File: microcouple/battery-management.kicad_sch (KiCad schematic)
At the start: 17 parts, among them Q1 AO3415, SW2 SW_SPDT_MSK12CO2, U3 MCP73831-2-OT, U4 LM3671MFX

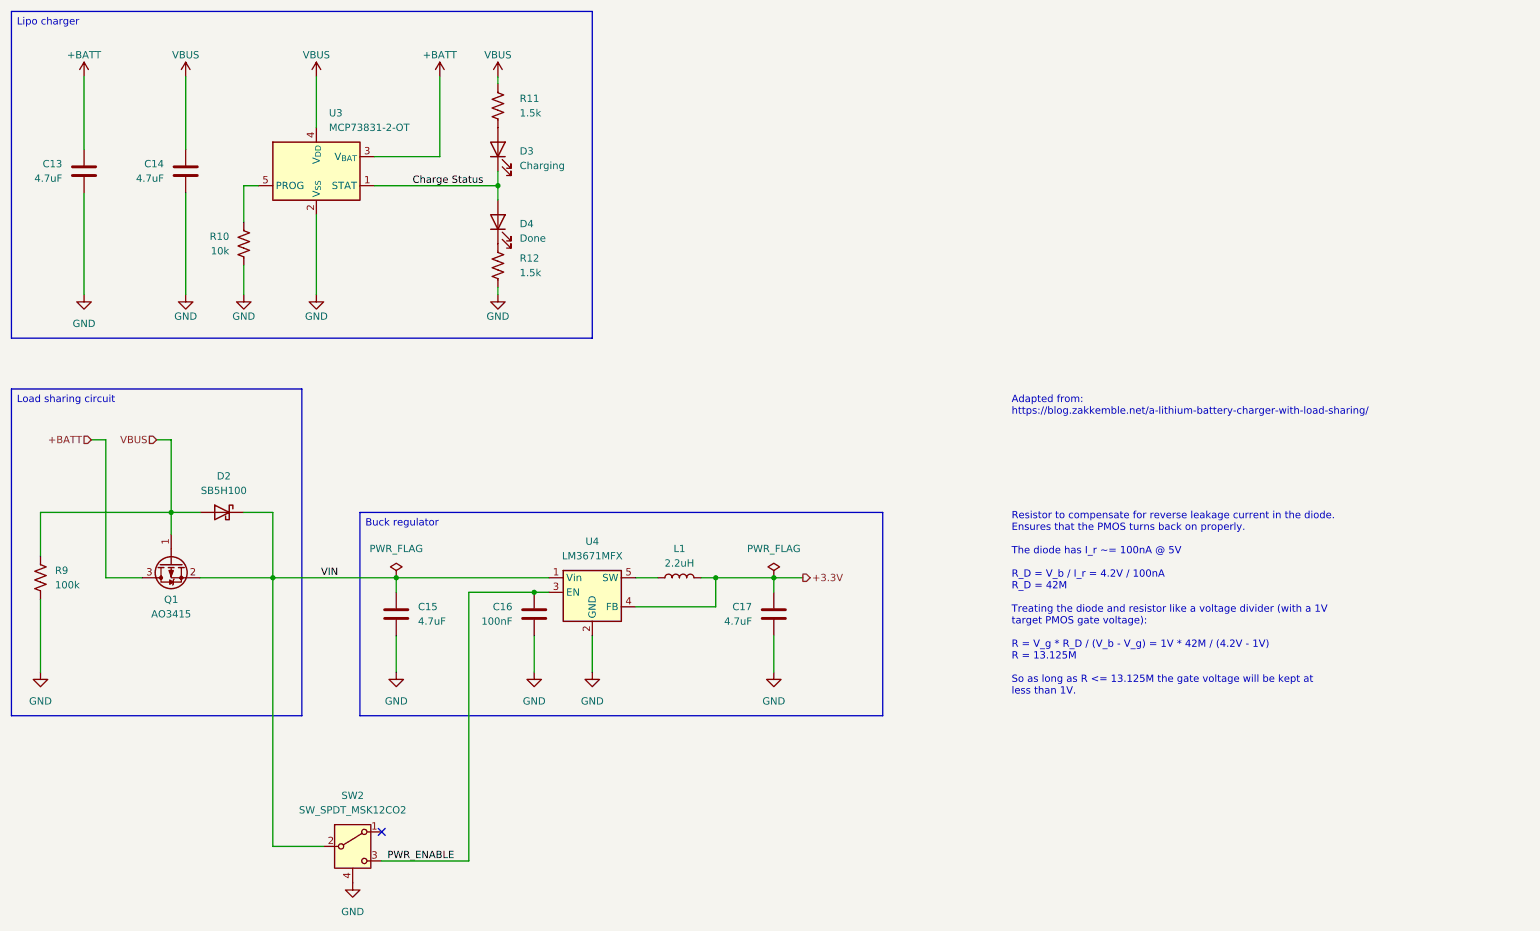
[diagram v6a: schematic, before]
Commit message: Update for JLCPCB
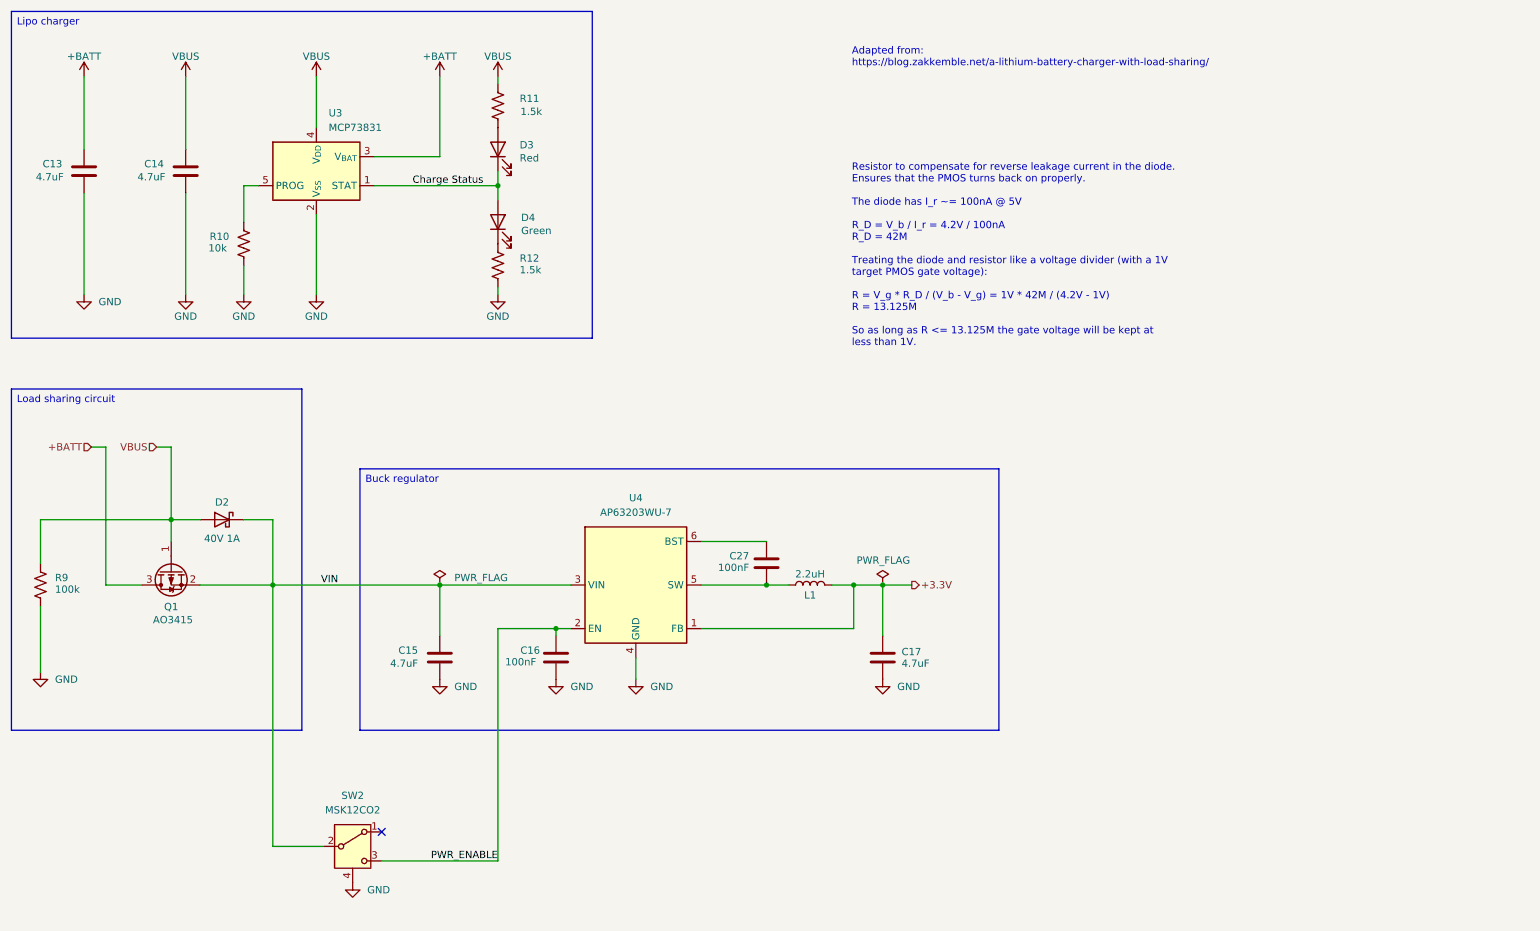
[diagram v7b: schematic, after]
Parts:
- added C27: 100nF, GS_Capacitors:C_0201_0603Metric, symbol GS_Capacitor_0201:C_0201_100nF
- C13, C14, C15, C17: footprint GS_SMD:0402_1005Metric -> GS_Capacitors:C_0402_1005Metric; symbol Device:C -> GS_Capacitor_0402:C_0402_4.7uF; LCSC ID (none) -> C76996; Manufacturer (none) -> Murata Electronics; Mfr. Part # (none) -> GRM155R60J475ME87D; Package (none) -> 0402
- C16: footprint GS_SMD:0201_0603Metric -> GS_Capacitors:C_0201_0603Metric; symbol Device:C -> GS_Capacitor_0201:C_0201_100nF; LCSC ID (none) -> C18164587; Manufacturer (none) -> CCTC; Mfr. Part # (none) -> TCC0201X5R104M250ZT; Package (none) -> 0201
- D2: value SB5H100 -> 40V 1A; footprint Diode_SMD:D_SMB -> Diode_SMD:D_SOD-123; symbol Diode:SB5H100 -> GS_Diodes:1N5819W; LCSC ID (none) -> C41431973; Manufacturer (none) -> GOODWORK; Mfr. Part # (none) -> 1N5819W; Package (none) -> SOD-123
- D3: value Charging -> Red; symbol Device:LED -> GS_Optoelectronic:LED_0201_Red; LCSC ID (none) -> C3646923; Manufacturer (none) -> XINGLIGHT; Mfr. Part # (none) -> XL-0201SURC; Package (none) -> 0201
- D4: value Done -> Green; symbol Device:LED -> GS_Optoelectronic:LED_0201_Green; LCSC ID (none) -> C3646922; Manufacturer (none) -> XINGLIGHT; Mfr. Part # (none) -> XL-0201UGC; Package (none) -> 0201
- L1: symbol Device:L -> GS_Inductors:L_1008_2.2uH; LCSC ID (none) -> C19634045; Manufacturer (none) -> APV; Mfr. Part # (none) -> PNR252012-2R2M; Package (none) -> 1008
- Q1: symbol Transistor_FET:AO3401A -> GS_Transistors:MOSFET_P-Ch_20V_4.8A_37mR; LCSC ID (none) -> C840839; Manufacturer (none) -> MDD(Microdiode Semiconductor); Mfr. Part # (none) -> AO3415; Package (none) -> SOT-23
- R10: footprint GS_SMD:0201_0603Metric -> GS_Resistors:R_0201_0603Metric; symbol Device:R_US -> GS_Resistor_0201:R_0201_10k; LCSC ID (none) -> C304504; Manufacturer (none) -> FH (Guangdong Fenghua Advanced Tech); Mfr. Part # (none) -> RC-01W103JT; Package (none) -> 0201
- R11, R12: footprint GS_SMD:0201_0603Metric -> GS_Resistors:R_0201_0603Metric; symbol Device:R_US -> GS_Resistor_0201:R_0201_1.5k; LCSC ID (none) -> C270328; Manufacturer (none) -> UNI-ROYAL(Uniroyal Elec); Mfr. Part # (none) -> 0201WMJ0152TEE; Package (none) -> 0201
- R9: footprint GS_SMD:0201_0603Metric -> GS_Resistors:R_0201_0603Metric; symbol Device:R_US -> GS_Resistor_0201:R_0201_100k; LCSC ID (none) -> C106224; Manufacturer (none) -> YAGEO; Mfr. Part # (none) -> RC0201FR-07100KL; Package (none) -> 0201
- SW2: value SW_SPDT_MSK12CO2 -> MSK12CO2; Manufacturer (none) -> SHOU HAN; Mfr. Part # (none) -> MINI MSK12CO2; Package (none) -> SMD
- U3: value MCP73831-2-OT -> MCP73831; symbol Battery_Management:MCP73831-2-OT -> GS_PMIC:MCP73831T-2ACI/OT; LCSC ID (none) -> C424093; Manufacturer (none) -> Microchip Tech; Mfr. Part # (none) -> MCP73831T-2ACI/OT; Package (none) -> SOT-23-5
- U4: value LM3671MFX -> AP63203WU-7; footprint Package_TO_SOT_SMD:TSOT-23-5 -> Package_TO_SOT_SMD:TSOT-23-6; symbol Regulator_Switching:LM3670MF -> GS_PMIC:AP63203WU-7; LCSC ID (none) -> C780769; Manufacturer (none) -> Diodes Incorporated; Mfr. Part # (none) -> AP63203WU-7; Package (none) -> TSOT-23-6
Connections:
- net +3.3V: now also U4.1 (FB); no longer U4.4 (FB)
- net GND: now also U4.4 (GND); no longer U4.2 (GND)
- net PWR_ENABLE: now also U4.2 (EN); no longer U4.3 (EN)
- net VIN: now also U4.3 (VIN); no longer U4.1 (Vin)
- net at L1.1, U4.5 (SW): now also C27.2
- new net: C27.1, U4.6 (BST)
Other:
- moved on the sheet: C15, C16, C17, D2, L1, Q1, R9

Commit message: Change all components to 0402 if smaller
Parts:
- C16, C27: footprint GS_Capacitors:C_0201_0603Metric -> GS_Capacitors:C_0402_1005Metric; symbol GS_Capacitor_0201:C_0201_100nF -> GS_Capacitor_0402:C_0402_100nF; LCSC ID C18164587 -> C344189; Mfr. Part # TCC0201X5R104M250ZT -> TCC0402X5R104K160AT; Package 0201 -> 0402
- D3: footprint GS_Optoelectronics:LED_0201_0603Metric -> GS_Optoelectronics:LED_0402_1005Metric; symbol GS_Optoelectronic:LED_0201_Red -> GS_Optoelectronic:LED_0402_Red; LCSC ID C3646923 -> C965790; Mfr. Part # XL-0201SURC -> XL-1005SURC; Package 0201 -> 0402
- D4: footprint GS_Optoelectronics:LED_0201_0603Metric -> GS_Optoelectronics:LED_0402_1005Metric; symbol GS_Optoelectronic:LED_0201_Green -> GS_Optoelectronic:LED_0402_Green; LCSC ID C3646922 -> C965793; Mfr. Part # XL-0201UGC -> XL-1005UGC; Package 0201 -> 0402
- R10: footprint GS_Resistors:R_0201_0603Metric -> GS_Resistors:R_0402_1005Metric; symbol GS_Resistor_0201:R_0201_10k -> GS_Resistor_0402:R_0402_10k; LCSC ID C304504 -> C102759; Manufacturer FH (Guangdong Fenghua Advanced Tech) -> RALEC; Mfr. Part # RC-01W103JT -> RTT02103JTH; Package 0201 -> 0402
- R11, R12: footprint GS_Resistors:R_0201_0603Metric -> GS_Resistors:R_0402_1005Metric; symbol GS_Resistor_0201:R_0201_1.5k -> GS_Resistor_0402:R_0402_1.5k; LCSC ID C270328 -> C2929900; Manufacturer UNI-ROYAL(Uniroyal Elec) -> FOJAN; Mfr. Part # 0201WMJ0152TEE -> FRC0402J152TS; Package 0201 -> 0402
- R9: footprint GS_Resistors:R_0201_0603Metric -> GS_Resistors:R_0402_1005Metric; symbol GS_Resistor_0201:R_0201_100k -> GS_Resistor_0402:R_0402_100k; LCSC ID C106224 -> C3017514; Manufacturer YAGEO -> VO; Mfr. Part # RC0201FR-07100KL -> SCR0402J100K; Package 0201 -> 0402
